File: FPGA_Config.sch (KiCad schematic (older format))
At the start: 2 parts

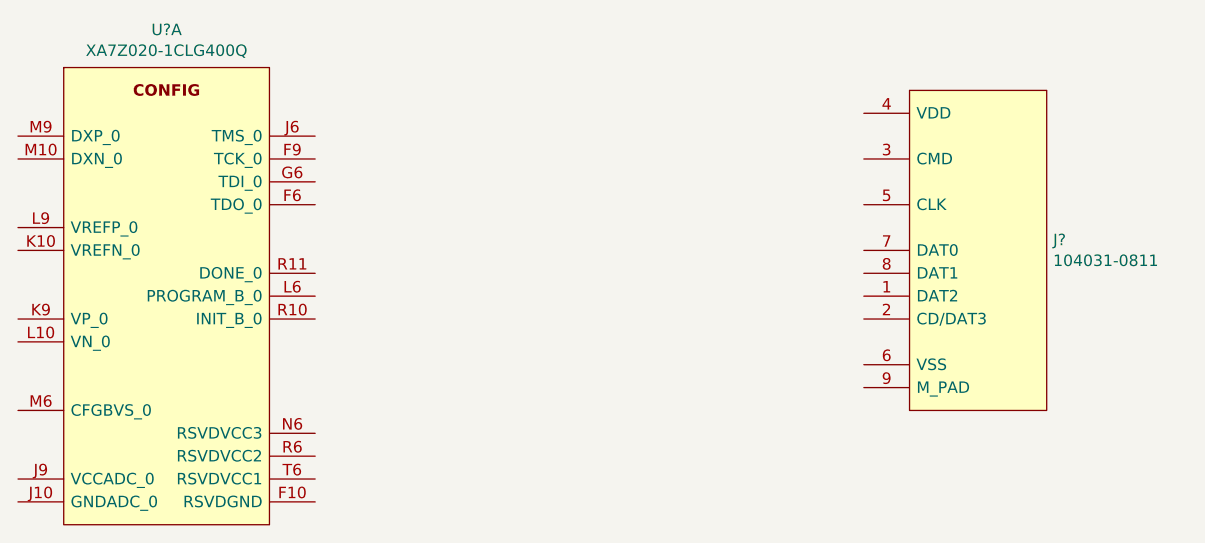
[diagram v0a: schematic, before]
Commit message: Completeed the FPGA_Power sheet Created PCB
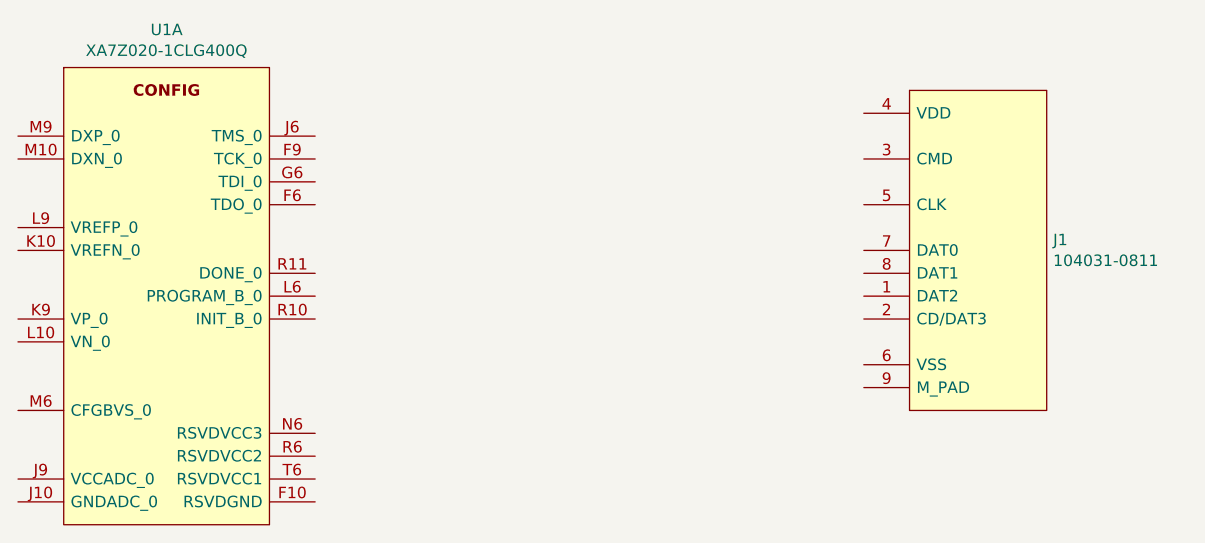
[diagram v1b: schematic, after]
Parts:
- gave numbers to parts that had none: 2
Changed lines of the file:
@@
 $EndDescr
 $Comp
-L GM_FPGA:XA7Z020-1CLG400Q U?
+L GM_FPGA:XA7Z020-1CLG400Q U1
 U 1 1 601B552F
 P 5400 2200
-F 0 "U?" H 5850 2365 50  0000 C CNN
+F 0 "U1" H 5850 2365 50  0000 C CNN
 F 1 "XA7Z020-1CLG400Q" H 5850 2274 50  0000 C CNN
 F 2 "BGA400C80P20X20_1700X1700X160" H 8250 2300 50  0001 L CNN
@@
 $EndComp
 $Comp
-L GM_Connectors:104031-0811 J?
+L GM_Connectors:104031-0811 J1
 U 1 1 601C79EF
 P 9100 2300
-F 0 "J?" H 9728 1646 50  0000 L CNN
+F 0 "J1" H 9728 1646 50  0000 L CNN
 F 1 "104031-0811" H 9728 1555 50  0000 L CNN
 F 2 "Connector_Card:microSD_HC_Molex_104031-0811" H 10950 2300 50  0001 L CNN
